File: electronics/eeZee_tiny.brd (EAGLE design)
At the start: 21.1 x 16.3 mm, 8 parts, among them IC1 ATtiny, J2 avrisp

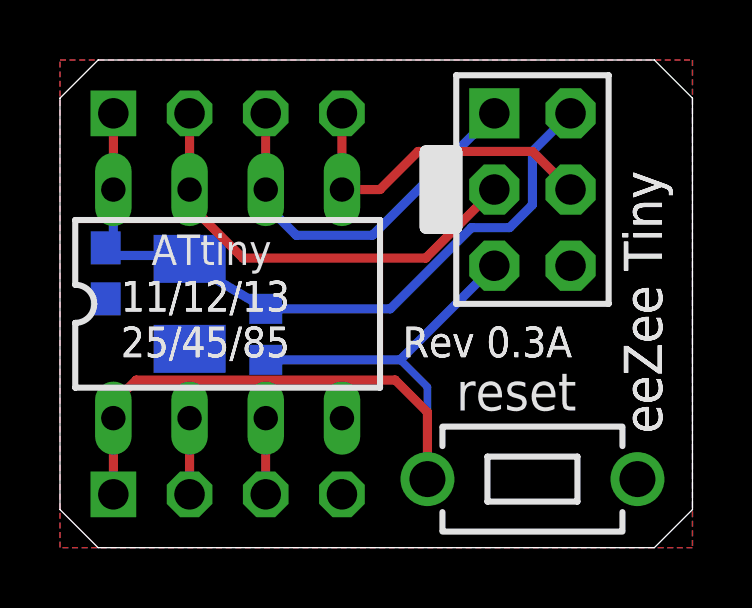
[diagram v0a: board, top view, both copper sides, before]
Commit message: revised 8pdip pads, rerouted avrisp traces, changed passives layout, changed main cap from 100u to 10u and changed to 1206 pkg, replaced attiny13 with attiny25 from bt library, changed avrisp to version from bt library, changed logo, added cc-by-sa, added documentation url
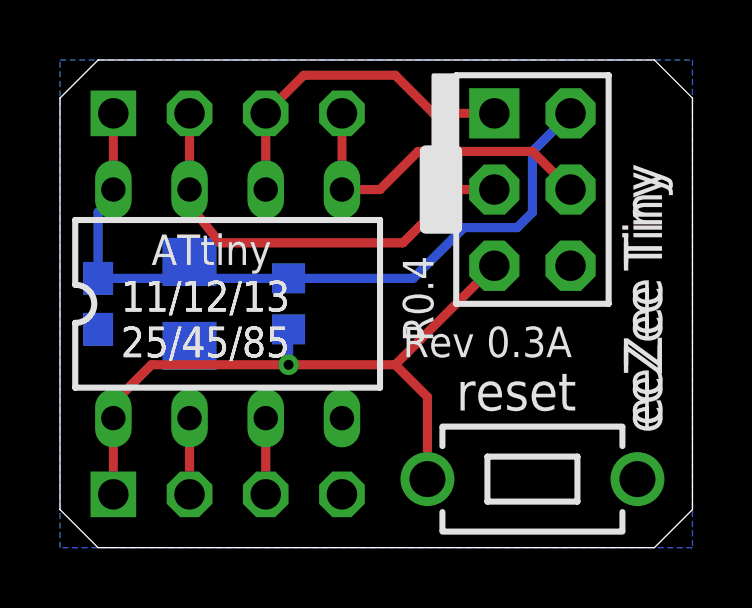
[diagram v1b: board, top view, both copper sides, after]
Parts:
- added U$1: BTLOGO-LOGO-MD, bt:BTLOGOM
- C1: value 0.1uF -> 104
- C2: value 100uF -> 106; device mes_rcl:SMC_B -> rcl:C1206
- IC1: device avr:DIL08 -> bt_avr:DIL08
- J2: device ads4:CON6P2R -> bt_avr:CON6P2R
- moved R1 1.27 mm to (7.62, 8.13)
- moved C1 1.05 mm to (1.27, 8.13)
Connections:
- net N$2 renamed PB3
- net N$8 renamed PB4
- net GND: now also C2.2; no longer C2.-
- net VCC: now also C2.1; no longer C2.+
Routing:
- net !RESET: track 29.8 -> 23.1 mm, vias 0 -> 1
- net MISO: track 12.8 -> 11.2 mm
- net VCC: track 24.6 -> 25.7 mm
- removed copper zone on layer 1, net GND
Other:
- board text added: "R0.4"
- board text added: "cc-by-sa"
- board text added: "goo.gl/0E6E8U"
